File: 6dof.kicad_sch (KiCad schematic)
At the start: 2 parts, among them IC2 BMI323

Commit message: added buck
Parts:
- added JP1: SolderJumper_3_Open, symbol Jumper:SolderJumper_3_Open
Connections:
- net +3V3: now also JP1.1 (A); no longer IC2.12 (CSB), IC2.5 (VDDIO), IC2.8 (VDD)
- new net: IC2.12 (CSB), IC2.5 (VDDIO), IC2.8 (VDD), JP1.2 (C)
- new net +1V8: JP1.3 (B)
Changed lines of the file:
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@@
+    (stroke (width 0) (type default))
+  )
+  (wire (pts (xy 186.69 111.76) (xy 186.69 127))
     (stroke (width 0) (type default))
   )
@@
     (stroke (width 0) (type default))
   )
+  (wire (pts (xy 209.55 105.41) (xy 217.17 105.41))
+    (stroke (width 0) (type default))
+  )
   (wire (pts (xy 184.15 134.62) (xy 189.23 134.62))
     (stroke (width 0) (type default))
@@
     (stroke (width 0) (type default))
   )
+  (wire (pts (xy 191.77 105.41) (xy 199.39 105.41))
+    (stroke (width 0) (type default))
+  )
   (wire (pts (xy 184.15 132.08) (xy 189.23 132.08))
     (stroke (width 0) (type default))
@@
     (stroke (width 0) (type default))
   )
+  (wire (pts (xy 186.69 111.76) (xy 204.47 111.76))
+    (stroke (width 0) (type default))
+  )
   (wire (pts (xy 186.69 139.7) (xy 189.23 139.7))
     (stroke (width 0) (type default))
@@
     (stroke (width 0) (type default))
   )
-  (wire (pts (xy 186.69 121.92) (xy 186.69 127))
+  (wire (pts (xy 217.17 97.79) (xy 217.17 105.41))
+    (stroke (width 0) (type default))
+  )
+  (wire (pts (xy 191.77 97.79) (xy 191.77 105.41))
     (stroke (width 0) (type default))
   )
@@
   (hierarchical_label "BMI_SCL" (shape input) (at 184.15 129.54 180) (fields_autoplaced)
     (effects (font (size 1.27 1.27)) (justify right))
+  )
+  (symbol (lib_id "Jumper:SolderJumper_3_Open") (at 204.47 105.41 0) (unit 1)
+    (in_bom yes) (on_board yes) (dnp no) (fields_autoplaced)
+    (property "Reference" "JP1" (at 204.47 100.33 0)
+      (effects (font (size 1.27 1.27)))
+    )
+    (property "Value" "SolderJumper_3_Open" (at 204.47 102.87 0)
+      (effects (font (size 1.27 1.27)))
+    )
+    (property "Footprint" "" (at 204.47 105.41 0)
+      (effects (font (size 1.27 1.27)) hide)
+    )
+    (property "Datasheet" "~" (at 204.47 105.41 0)
+      (effects (font (size 1.27 1.27)) hide)
+    )
+    (pin "1")
+    (pin "2")
+    (pin "3")
+    (instances
+      (project "armband"
+        (path "/017c50c6-333c-4d31-ad5a-278994a09b14/2935dd4b-68c9-428b-bdab-ba656d5b03fa"
+          (reference "JP1") (unit 1)
+        )
+      )
+    )
   )
   (symbol (lib_id "ARMband:BMI323") (at 189.23 129.54 0) (unit 1)
@@
   (symbol (lib_id "power:GND") (at 204.47 160.02 0) (unit 1)
     (in_bom yes) (on_board yes) (dnp no) (fields_autoplaced)
-    (property "Reference" "#PWR017" (at 204.47 166.37 0)
+    (property "Reference" "#PWR020" (at 204.47 166.37 0)
       (effects (font (size 1.27 1.27)) hide)
     )
@@
       (project "armband"
         (path "/017c50c6-333c-4d31-ad5a-278994a09b14/2935dd4b-68c9-428b-bdab-ba656d5b03fa"
-          (reference "#PWR017") (unit 1)
-        )
-      )
-    )
-  )
-  (symbol (lib_id "power:+3V3") (at 204.47 109.22 0) (unit 1)
-    (in_bom yes) (on_board yes) (dnp no) (fields_autoplaced)
-    (property "Reference" "#PWR016" (at 204.47 113.03 0)
-      (effects (font (size 1.27 1.27)) hide)
-    )
-    (property "Value" "+3V3" (at 204.47 105.41 0)
-      (effects (font (size 1.27 1.27)))
-    )
-    (property "Footprint" "" (at 204.47 109.22 0)
-      (effects (font (size 1.27 1.27)) hide)
-    )
-    (property "Datasheet" "" (at 204.47 109.22 0)
-      (effects (font (size 1.27 1.27)) hide)
-    )
-    (pin "1")
-    (instances
-      (project "armband"
-        (path "/017c50c6-333c-4d31-ad5a-278994a09b14/2935dd4b-68c9-428b-bdab-ba656d5b03fa"
-          (reference "#PWR016") (unit 1)
+          (reference "#PWR020") (unit 1)
+        )
+      )
+    )
+  )
+  (symbol (lib_id "power:+1V8") (at 217.17 97.79 0) (unit 1)
+    (in_bom yes) (on_board yes) (dnp no) (fields_autoplaced)
+    (property "Reference" "#PWR014" (at 217.17 101.6 0)
+      (effects (font (size 1.27 1.27)) hide)
+    )
+    (property "Value" "+1V8" (at 217.17 93.98 0)
+      (effects (font (size 1.27 1.27)))
+    )
+    (property "Footprint" "" (at 217.17 97.79 0)
+      (effects (font (size 1.27 1.27)) hide)
+    )
+    (property "Datasheet" "" (at 217.17 97.79 0)
+      (effects (font (size 1.27 1.27)) hide)
+    )
+    (pin "1")
+    (instances
+      (project "armband"
+        (path "/017c50c6-333c-4d31-ad5a-278994a09b14/2935dd4b-68c9-428b-bdab-ba656d5b03fa"
+          (reference "#PWR014") (unit 1)
+        )
+      )
+    )
+  )
+  (symbol (lib_id "power:+3V3") (at 191.77 97.79 0) (unit 1)
+    (in_bom yes) (on_board yes) (dnp no) (fields_autoplaced)
+    (property "Reference" "#PWR019" (at 191.77 101.6 0)
+      (effects (font (size 1.27 1.27)) hide)
+    )
+    (property "Value" "+3V3" (at 191.77 93.98 0)
+      (effects (font (size 1.27 1.27)))
+    )
+    (property "Footprint" "" (at 191.77 97.79 0)
+      (effects (font (size 1.27 1.27)) hide)
+    )
+    (property "Datasheet" "" (at 191.77 97.79 0)
+      (effects (font (size 1.27 1.27)) hide)
+    )
+    (pin "1")
+    (instances
+      (project "armband"
+        (path "/017c50c6-333c-4d31-ad5a-278994a09b14/2935dd4b-68c9-428b-bdab-ba656d5b03fa"
+          (reference "#PWR019") (unit 1)
         )
       )
@@
     )
   )
-  (symbol (lib_id "power:+3V3") (at 186.69 121.92 0) (unit 1)
-    (in_bom yes) (on_board yes) (dnp no) (fields_autoplaced)
-    (property "Reference" "#PWR014" (at 186.69 125.73 0)
-      (effects (font (size 1.27 1.27)) hide)
-    )
-    (property "Value" "+3V3" (at 186.69 118.11 0)
-      (effects (font (size 1.27 1.27)))
-    )
-    (property "Footprint" "" (at 186.69 121.92 0)
-      (effects (font (size 1.27 1.27)) hide)
-    )
-    (property "Datasheet" "" (at 186.69 121.92 0)
-      (effects (font (size 1.27 1.27)) hide)
-    )
-    (pin "1")
-    (instances
-      (project "armband"
-        (path "/017c50c6-333c-4d31-ad5a-278994a09b14/2935dd4b-68c9-428b-bdab-ba656d5b03fa"
-          (reference "#PWR014") (unit 1)
-        )
-      )
-    )
-  )
   (symbol (lib_id "power:GND") (at 186.69 149.86 0) (mirror y) (unit 1)
     (in_bom yes) (on_board yes) (dnp no) (fields_autoplaced)
-    (property "Reference" "#PWR015" (at 186.69 156.21 0)
+    (property "Reference" "#PWR018" (at 186.69 156.21 0)
       (effects (font (size 1.27 1.27)) hide)
     )
@@
       (project "armband"
         (path "/017c50c6-333c-4d31-ad5a-278994a09b14/2935dd4b-68c9-428b-bdab-ba656d5b03fa"
-          (reference "#PWR015") (unit 1)
-        )
-      )
+          (reference "#PWR018") (unit 1)
+        )
+      )

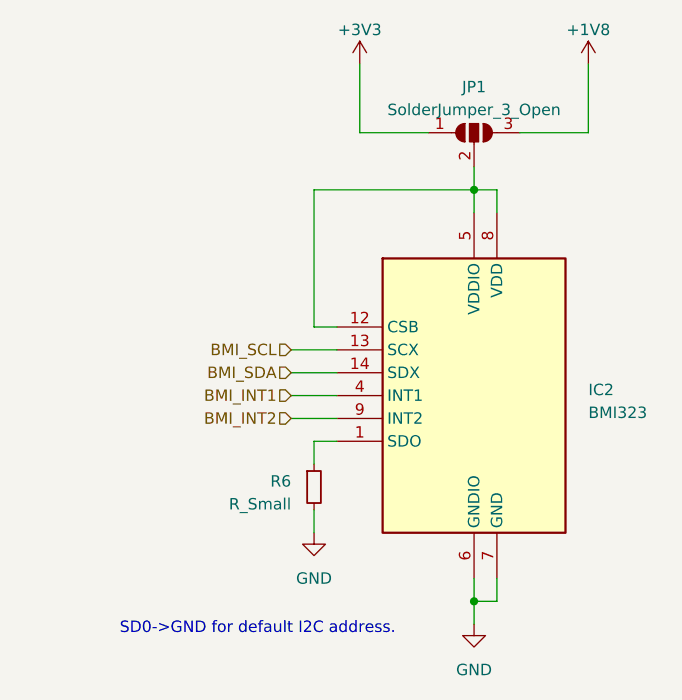
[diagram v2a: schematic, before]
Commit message: added decoupling capacitors to sensors
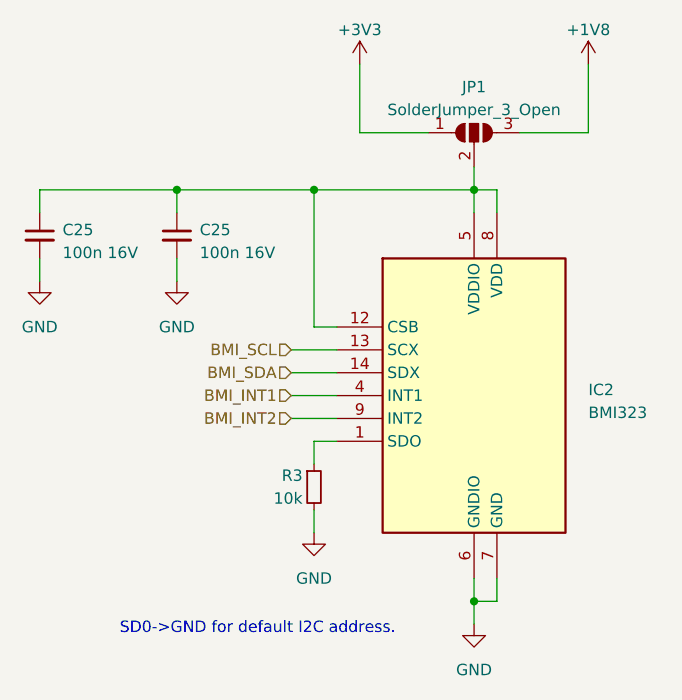
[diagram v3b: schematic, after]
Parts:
- removed R6: R_Small, symbol Device:R_Small
- added C25 (x2): 100n 16V, Capacitor_SMD:C_0402_1005Metric, symbol Device:C_Small
- added R3: 10k, Resistor_SMD:R_0201_0603Metric_Pad0.64x0.40mm_HandSolder, symbol Device:R_Small
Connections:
- net GND: now also C25.2, C25.2, R3.2
- net at IC2.12 (CSB), IC2.5 (VDDIO), IC2.8 (VDD)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: now also C25.1, C25.1
- net at IC2.1 (SDO): now also R3.1
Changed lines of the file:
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@@
 (kicad_sch (version 20230121) (generator eeschema)
   (paper "A3")
+  (junction (at 186.69 111.76) (diameter 0) (color 0 0 0 0)
+  )
   (junction (at 204.47 111.76) (diameter 0) (color 0 0 0 0)
   )
   (junction (at 204.47 157.48) (diameter 0) (color 0 0 0 0)
   )
+  (junction (at 171.45 111.76) (diameter 0) (color 0 0 0 0)
+  )
   (wire (pts (xy 204.47 111.76) (xy 204.47 114.3))
     (stroke (width 0) (type default))
@@
     (stroke (width 0) (type default))
   )
+  (wire (pts (xy 156.21 119.38) (xy 156.21 121.92))
+    (stroke (width 0) (type default))
+  )
+  (wire (pts (xy 171.45 111.76) (xy 186.69 111.76))
+    (stroke (width 0) (type default))
+  )
   (wire (pts (xy 207.01 114.3) (xy 207.01 111.76))
     (stroke (width 0) (type default))
   )
+  (wire (pts (xy 171.45 119.38) (xy 171.45 121.92))
+    (stroke (width 0) (type default))
+  )
   (wire (pts (xy 191.77 105.41) (xy 199.39 105.41))
     (stroke (width 0) (type default))
   )
+  (wire (pts (xy 156.21 114.3) (xy 156.21 111.76))
+    (stroke (width 0) (type default))
+  )
   (wire (pts (xy 184.15 132.08) (xy 189.23 132.08))
     (stroke (width 0) (type default))
   )
+  (wire (pts (xy 171.45 114.3) (xy 171.45 111.76))
+    (stroke (width 0) (type default))
+  )
   (wire (pts (xy 186.69 147.32) (xy 186.69 149.86))
     (stroke (width 0) (type default))
@@
   )
   (wire (pts (xy 204.47 154.94) (xy 204.47 157.48))
+    (stroke (width 0) (type default))
+  )
+  (wire (pts (xy 156.21 111.76) (xy 171.45 111.76))
     (stroke (width 0) (type default))
   )
@@
     (effects (font (size 1.27 1.27)) (justify right))
   )
+  (symbol (lib_id "power:GND") (at 171.45 121.92 0) (unit 1)
+    (in_bom yes) (on_board yes) (dnp no) (fields_autoplaced)
+    (property "Reference" "#PWR036" (at 171.45 128.27 0)
+      (effects (font (size 1.27 1.27)) hide)
+    )
+    (property "Value" "GND" (at 171.45 127 0)
+      (effects (font (size 1.27 1.27)))
+    )
+    (property "Footprint" "" (at 171.45 121.92 0)
+      (effects (font (size 1.27 1.27)) hide)
+    )
+    (property "Datasheet" "" (at 171.45 121.92 0)
+      (effects (font (size 1.27 1.27)) hide)
+    )
+    (pin "1")
+    (instances
+      (project "armband"
+        (path "/017c50c6-333c-4d31-ad5a-278994a09b14/2935dd4b-68c9-428b-bdab-ba656d5b03fa"
+          (reference "#PWR036") (unit 1)
+        )
+      )
+    )
+  )
   (symbol (lib_id "Jumper:SolderJumper_3_Open") (at 204.47 105.41 0) (unit 1)
     (in_bom yes) (on_board yes) (dnp no) (fields_autoplaced)
@@
         (path "/017c50c6-333c-4d31-ad5a-278994a09b14/2935dd4b-68c9-428b-bdab-ba656d5b03fa"
           (reference "JP1") (unit 1)
+        )
+      )
+    )
+  )
+  (symbol (lib_id "Device:C_Small") (at 171.45 116.84 0) (mirror y) (unit 1)
+    (in_bom yes) (on_board yes) (dnp no)
+    (property "Reference" "C25" (at 173.99 116.2113 0)
+      (effects (font (size 1.27 1.27)) (justify right))
+    )
+    (property "Value" "100n 16V" (at 173.99 118.7513 0)
+      (effects (font (size 1.27 1.27)) (justify right))
+    )
+    (property "Footprint" "Capacitor_SMD:C_0402_1005Metric" (at 171.45 116.84 0)
+      (effects (font (size 1.27 1.27)) hide)
+    )
+    (property "Datasheet" "https://www.mouser.de/datasheet/2/447/KEM_C1005_Y5V_SMD-3316374.pdf" (at 171.45 116.84 0)
+      (effects (font (size 1.27 1.27)) hide)
+    )
+    (property "MFN" "80-C0402C104M4V " (at 171.45 116.84 0)
+      (effects (font (size 1.27 1.27)) hide)
+    )
+    (pin "1")
+    (pin "2")
+    (instances
+      (project "armband"
+        (path "/017c50c6-333c-4d31-ad5a-278994a09b14"
+          (reference "C25") (unit 1)
+        )
+        (path "/017c50c6-333c-4d31-ad5a-278994a09b14/ae5dc462-dca9-40e4-ba02-6b87a86a4904"
+          (reference "C14") (unit 1)
+        )
+        (path "/017c50c6-333c-4d31-ad5a-278994a09b14/db6ac415-a2f9-4935-934d-f0e91f8b44d3"
+          (reference "C12") (unit 1)
+        )
+        (path "/017c50c6-333c-4d31-ad5a-278994a09b14/2935dd4b-68c9-428b-bdab-ba656d5b03fa"
+          (reference "C15") (unit 1)
         )
       )
@@
     )
   )
+  (symbol (lib_id "power:GND") (at 156.21 121.92 0) (unit 1)
+    (in_bom yes) (on_board yes) (dnp no) (fields_autoplaced)
+    (property "Reference" "#PWR049" (at 156.21 128.27 0)
+      (effects (font (size 1.27 1.27)) hide)
+    )
+    (property "Value" "GND" (at 156.21 127 0)
+      (effects (font (size 1.27 1.27)))
+    )
+    (property "Footprint" "" (at 156.21 121.92 0)
+      (effects (font (size 1.27 1.27)) hide)
+    )
+    (property "Datasheet" "" (at 156.21 121.92 0)
+      (effects (font (size 1.27 1.27)) hide)
+    )
+    (pin "1")
+    (instances
+      (project "armband"
+        (path "/017c50c6-333c-4d31-ad5a-278994a09b14/2935dd4b-68c9-428b-bdab-ba656d5b03fa"
+          (reference "#PWR049") (unit 1)
+        )
+      )
+    )
+  )
+  (symbol (lib_id "Device:C_Small") (at 156.21 116.84 0) (mirror y) (unit 1)
+    (in_bom yes) (on_board yes) (dnp no)
+    (property "Reference" "C25" (at 158.75 116.2113 0)
+      (effects (font (size 1.27 1.27)) (justify right))
+    )
+    (property "Value" "100n 16V" (at 158.75 118.7513 0)
+      (effects (font (size 1.27 1.27)) (justify right))
+    )
+    (property "Footprint" "Capacitor_SMD:C_0402_1005Metric" (at 156.21 116.84 0)
+      (effects (font (size 1.27 1.27)) hide)
+    )
+    (property "Datasheet" "https://www.mouser.de/datasheet/2/447/KEM_C1005_Y5V_SMD-3316374.pdf" (at 156.21 116.84 0)
+      (effects (font (size 1.27 1.27)) hide)
+    )
+    (property "MFN" "80-C0402C104M4V " (at 156.21 116.84 0)
+      (effects (font (size 1.27 1.27)) hide)
+    )
+    (pin "1")
+    (pin "2")
+    (instances
+      (project "armband"
+        (path "/017c50c6-333c-4d31-ad5a-278994a09b14"
+          (reference "C25") (unit 1)
+        )
+        (path "/017c50c6-333c-4d31-ad5a-278994a09b14/ae5dc462-dca9-40e4-ba02-6b87a86a4904"
+          (reference "C14") (unit 1)
+        )
+        (path "/017c50c6-333c-4d31-ad5a-278994a09b14/db6ac415-a2f9-4935-934d-f0e91f8b44d3"
+          (reference "C12") (unit 1)
+        )
+        (path "/017c50c6-333c-4d31-ad5a-278994a09b14/2935dd4b-68c9-428b-bdab-ba656d5b03fa"
+          (reference "C16") (unit 1)
+        )
+      )
+    )
+  )
   (symbol (lib_id "power:+3V3") (at 191.77 97.79 0) (unit 1)
     (in_bom yes) (on_board yes) (dnp no) (fields_autoplaced)
@@
   )
   (symbol (lib_id "Device:R_Small") (at 186.69 144.78 0) (unit 1)
-    (in_bom yes) (on_board yes) (dnp no) (fields_autoplaced)
-    (property "Reference" "R6" (at 184.15 144.145 0)
-      (effects (font (size 1.27 1.27)) (justify right))
-    )
-    (property "Value" "R_Small" (at 184.15 146.685 0)
-      (effects (font (size 1.27 1.27)) (justify right))
-    )
-    (property "Footprint" "" (at 186.69 144.78 0)
-      (effects (font (size 1.27 1.27)) hide)
-    )
-    (property "Datasheet" "~" (at 186.69 144.78 0)
+    (in_bom yes) (on_board yes) (dnp no)
+    (property "Reference" "R3" (at 185.42 143.51 0)
+      (effects (font (size 1.27 1.27)) (justify right))
+    )
+    (property "Value" "10k" (at 185.42 146.05 0)
+      (effects (font (size 1.27 1.27)) (justify right))
+    )
+    (property "Footprint" "Resistor_SMD:R_0201_0603Metric_Pad0.64x0.40mm_HandSolder" (at 186.69 144.78 0)
+      (effects (font (size 1.27 1.27)) hide)
+    )
+    (property "Datasheet" "https://www.mouser.de/datasheet/2/315/AOA0000C301-1488782.pdf" (at 186.69 144.78 0)
+      (effects (font (size 1.27 1.27)) hide)
+    )
+    (property "MFN" "667-ERJ-1GNJ103C " (at 186.69 144.78 0)
       (effects (font (size 1.27 1.27)) hide)
     )
@@
     (instances
       (project "armband"
-        (path "/017c50c6-333c-4d31-ad5a-278994a09b14/2935dd4b-68c9-428b-bdab-ba656d5b03fa"
-          (reference "R6") (unit 1)
-        )
-      )
+        (path "/017c50c6-333c-4d31-ad5a-278994a09b14"
+          (reference "R3") (unit 1)
+        )
+        (path "/017c50c6-333c-4d31-ad5a-278994a09b14/ae5dc462-dca9-40e4-ba02-6b87a86a4904"
+          (reference "R15") (unit 1)
+        )
+        (path "/017c50c6-333c-4d31-ad5a-278994a09b14/2935dd4b-68c9-428b-bdab-ba656d5b03fa"
+          (reference "R11") (unit 1)
+        )
+      )

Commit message: cleaned up symbol fields table and removed unused or duplicate fields.
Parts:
- IC2: MFN (none) -> 262-BMI323; Manufacturer_Name BOSCH -> (none); Manufacturer_Part_Number BMI323 -> (none); Mouser Part Number 262-BMI323 -> (none); Mouser Price/Stock https://www.mouser.co.uk/ProductDetail/Bosch-Sensortec/BMI3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 -> (none)
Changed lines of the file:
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@@
   (symbol (lib_id "power:GND") (at 171.45 121.92 0) (unit 1)
     (in_bom yes) (on_board yes) (dnp no) (fields_autoplaced)
-    (property "Reference" "#PWR036" (at 171.45 128.27 0)
+    (property "Reference" "#PWR022" (at 171.45 128.27 0)
       (effects (font (size 1.27 1.27)) hide)
     )
@@
       (project "armband"
         (path "/017c50c6-333c-4d31-ad5a-278994a09b14/2935dd4b-68c9-428b-bdab-ba656d5b03fa"
-          (reference "#PWR036") (unit 1)
+          (reference "#PWR022") (unit 1)
         )
       )
@@
         )
         (path "/017c50c6-333c-4d31-ad5a-278994a09b14/2935dd4b-68c9-428b-bdab-ba656d5b03fa"
-          (reference "C15") (unit 1)
+          (reference "C8") (unit 1)
         )
       )
@@
       (effects (font (size 1.27 1.27)) (justify left top) hide)
     )
-    (property "Mouser Part Number" "262-BMI323" (at 215.9 616.84 0)
-      (effects (font (size 1.27 1.27)) (justify left top) hide)
-    )
-    (property "Mouser Price/Stock" "https://www.mouser.co.uk/ProductDetail/Bosch-Sensortec/BMI323?qs=By6Nw2ByBD3%2FE1v0UqNQPQ%3D%3D" (at 215.9 716.84 0)
-      (effects (font (size 1.27 1.27)) (justify left top) hide)
-    )
-    (property "Manufacturer_Name" "BOSCH" (at 215.9 816.84 0)
-      (effects (font (size 1.27 1.27)) (justify left top) hide)
-    )
-    (property "Manufacturer_Part_Number" "BMI323" (at 215.9 916.84 0)
-      (effects (font (size 1.27 1.27)) (justify left top) hide)
+    (property "MFN" "262-BMI323" (at 189.23 129.54 0)
+      (effects (font (size 1.27 1.27)) hide)
     )
     (pin "1")
@@
   (symbol (lib_id "power:GND") (at 204.47 160.02 0) (unit 1)
     (in_bom yes) (on_board yes) (dnp no) (fields_autoplaced)
-    (property "Reference" "#PWR020" (at 204.47 166.37 0)
+    (property "Reference" "#PWR024" (at 204.47 166.37 0)
       (effects (font (size 1.27 1.27)) hide)
     )
@@
       (project "armband"
         (path "/017c50c6-333c-4d31-ad5a-278994a09b14/2935dd4b-68c9-428b-bdab-ba656d5b03fa"
+          (reference "#PWR024") (unit 1)
+        )
+      )
+    )
+  )
+  (symbol (lib_id "power:+1V8") (at 217.17 97.79 0) (unit 1)
+    (in_bom yes) (on_board yes) (dnp no) (fields_autoplaced)
+    (property "Reference" "#PWR020" (at 217.17 101.6 0)
+      (effects (font (size 1.27 1.27)) hide)
+    )
+    (property "Value" "+1V8" (at 217.17 93.98 0)
+      (effects (font (size 1.27 1.27)))
+    )
+    (property "Footprint" "" (at 217.17 97.79 0)
+      (effects (font (size 1.27 1.27)) hide)
+    )
+    (property "Datasheet" "" (at 217.17 97.79 0)
+      (effects (font (size 1.27 1.27)) hide)
+    )
+    (pin "1")
+    (instances
+      (project "armband"
+        (path "/017c50c6-333c-4d31-ad5a-278994a09b14/2935dd4b-68c9-428b-bdab-ba656d5b03fa"
           (reference "#PWR020") (unit 1)
         )
@@
     )
   )
-  (symbol (lib_id "power:+1V8") (at 217.17 97.79 0) (unit 1)
-    (in_bom yes) (on_board yes) (dnp no) (fields_autoplaced)
-    (property "Reference" "#PWR014" (at 217.17 101.6 0)
-      (effects (font (size 1.27 1.27)) hide)
-    )
-    (property "Value" "+1V8" (at 217.17 93.98 0)
-      (effects (font (size 1.27 1.27)))
-    )
-    (property "Footprint" "" (at 217.17 97.79 0)
-      (effects (font (size 1.27 1.27)) hide)
-    )
-    (property "Datasheet" "" (at 217.17 97.79 0)
-      (effects (font (size 1.27 1.27)) hide)
-    )
-    (pin "1")
-    (instances
-      (project "armband"
-        (path "/017c50c6-333c-4d31-ad5a-278994a09b14/2935dd4b-68c9-428b-bdab-ba656d5b03fa"
-          (reference "#PWR014") (unit 1)
-        )
-      )
-    )
-  )
   (symbol (lib_id "power:GND") (at 156.21 121.92 0) (unit 1)
     (in_bom yes) (on_board yes) (dnp no) (fields_autoplaced)
-    (property "Reference" "#PWR049" (at 156.21 128.27 0)
+    (property "Reference" "#PWR021" (at 156.21 128.27 0)
       (effects (font (size 1.27 1.27)) hide)
     )
@@
       (project "armband"
         (path "/017c50c6-333c-4d31-ad5a-278994a09b14/2935dd4b-68c9-428b-bdab-ba656d5b03fa"
-          (reference "#PWR049") (unit 1)
+          (reference "#PWR021") (unit 1)
         )
       )
@@
         )
         (path "/017c50c6-333c-4d31-ad5a-278994a09b14/2935dd4b-68c9-428b-bdab-ba656d5b03fa"
-          (reference "C16") (unit 1)
+          (reference "C7") (unit 1)
         )
       )
@@
         )
         (path "/017c50c6-333c-4d31-ad5a-278994a09b14/2935dd4b-68c9-428b-bdab-ba656d5b03fa"
-          (reference "R11") (unit 1)
+          (reference "R6") (unit 1)
         )
       )
@@
   (symbol (lib_id "power:GND") (at 186.69 149.86 0) (mirror y) (unit 1)
     (in_bom yes) (on_board yes) (dnp no) (fields_autoplaced)
-    (property "Reference" "#PWR018" (at 186.69 156.21 0)
+    (property "Reference" "#PWR023" (at 186.69 156.21 0)
       (effects (font (size 1.27 1.27)) hide)
     )
@@
       (project "armband"
         (path "/017c50c6-333c-4d31-ad5a-278994a09b14/2935dd4b-68c9-428b-bdab-ba656d5b03fa"
-          (reference "#PWR018") (unit 1)
-        )
-      )
+          (reference "#PWR023") (unit 1)
+        )
+      )
